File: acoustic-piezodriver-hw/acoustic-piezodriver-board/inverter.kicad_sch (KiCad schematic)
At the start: 35 parts, among them Q1 Si7450DP, Q2 Si7450DP, Q3 Si7450DP, Q4 Si7450DP, U1 UCC27282DR, U2 UCC27282DR

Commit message: [carrier] Added decoupling for DDR (next) Finish power supply
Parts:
- C10: Manufacturing Part Number (none) -> CL05B103KB5NNNC
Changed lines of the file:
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@@
+			)
+		)
+		(property "Manufacturing Part Number" "CL05B103KB5NNNC"
+			(at 125.73 96.52 0)
+			(effects
+				(font
+					(size 1.27 1.27)
+				)
+				(hide yes)
 			)
 		)

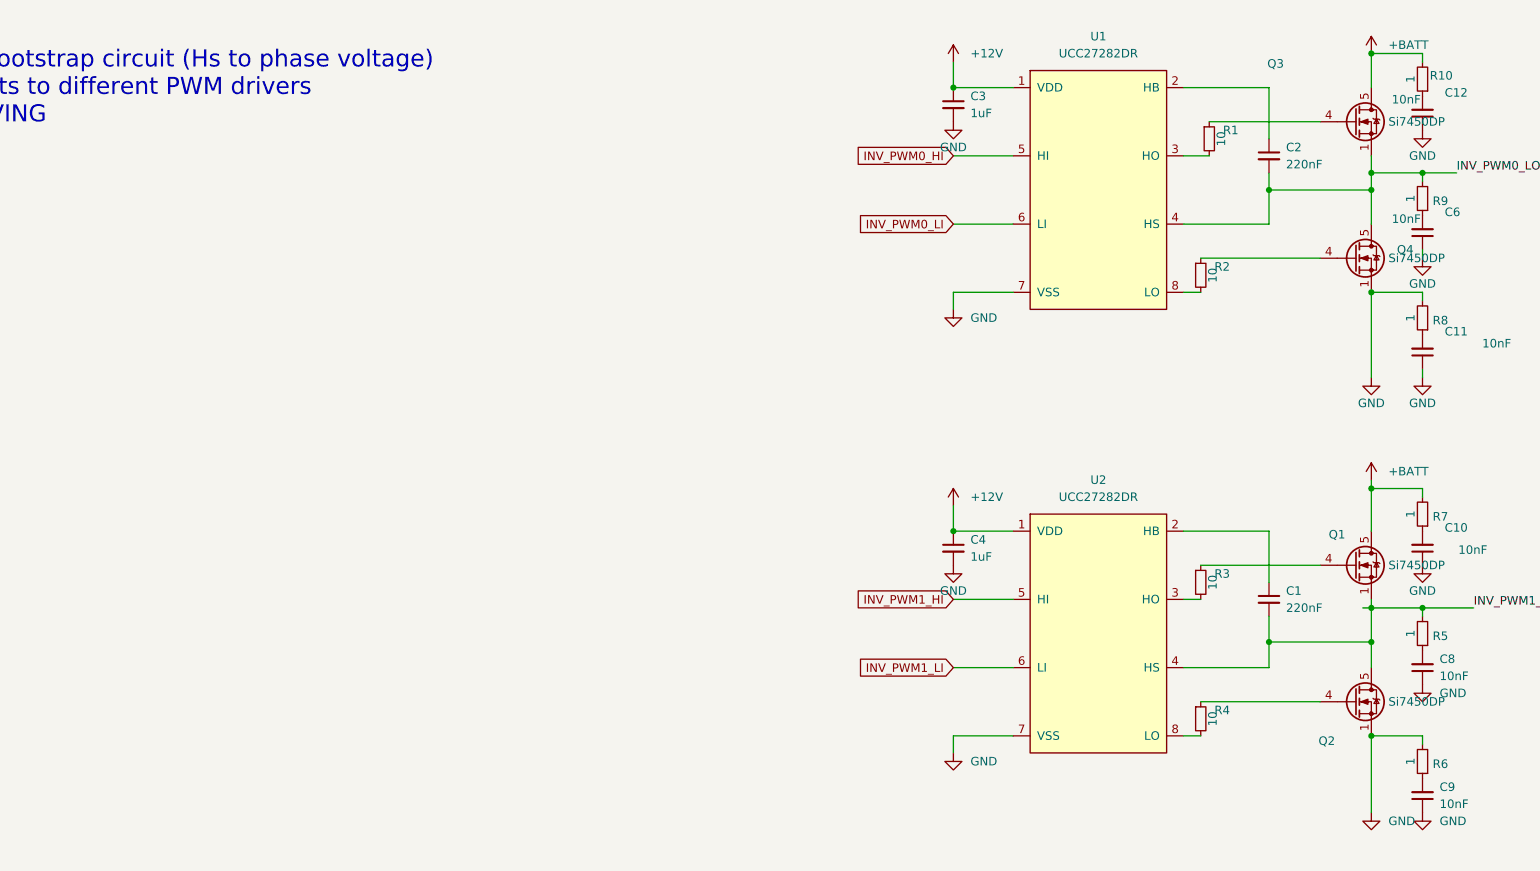
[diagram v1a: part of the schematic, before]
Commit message: [carrier] Added usb power + communication circuitry (next) Connect ADC pins to bank 0, select PWM pins, check connectors for power board
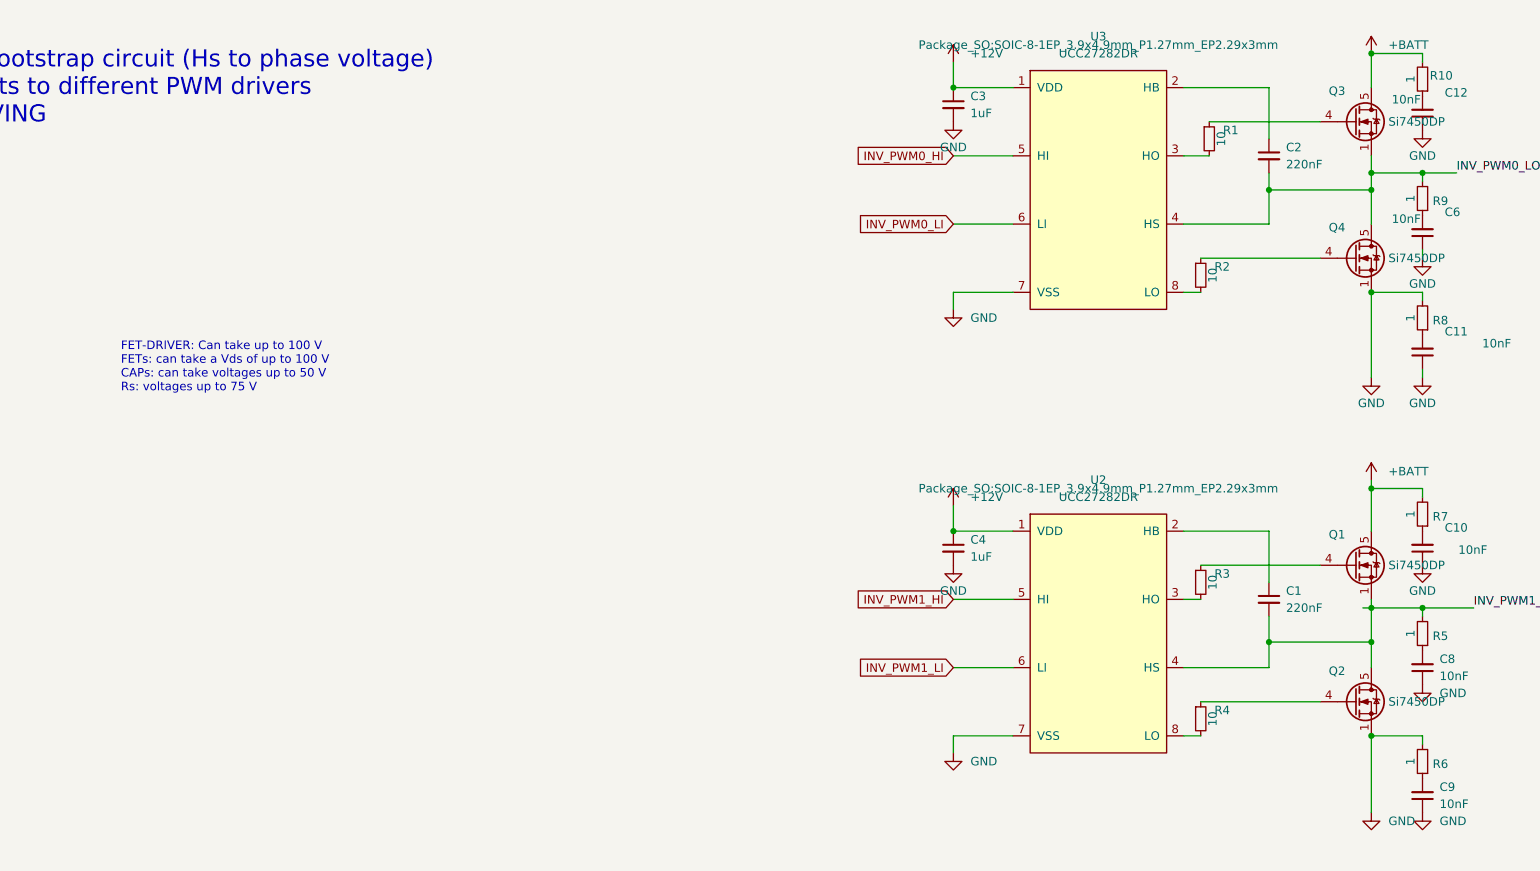
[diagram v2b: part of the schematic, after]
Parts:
- removed U1: UCC27282DR, symbol ucc27282:UCC27282DR
- added U3: UCC27282DR, Package_SO:SOIC-8-1EP_3.9x4.9mm_P1.27mm_EP2.29x3mm, symbol ucc27282:UCC27282DR
- Q1, Q2, Q3, Q4: LCSC Part Number C3289463 -> (none); LPN (none) -> C3289463; MPN (none) -> SI7454FDP-T1-RE3
- U2: footprint (none) -> Package_SO:SOIC-8-1EP_3.9x4.9mm_P1.27mm_EP2.29x3mm; MPN (none) -> UCC27282DR
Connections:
- net +12V: now also U3.1 (VDD)
- net GND: now also U3.7 (VSS)
- net INV_PWM0_HI: now also U3.5 (HI)
- net INV_PWM0_LI: now also U3.6 (LI)
- net INV_PWM0_LOAD: now also U3.4 (HS)
- net at R2.2: now also U3.8 (LO)
- net at C2.1: now also U3.2 (HB)
- net at R1.2: now also U3.3 (HO)
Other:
- note added: "FET-DRIVER: Can take up to 100 V FETs: can take a Vds of up to 100 V CAPs: can take voltages up to 50 V Rs: voltages up to 75 V"

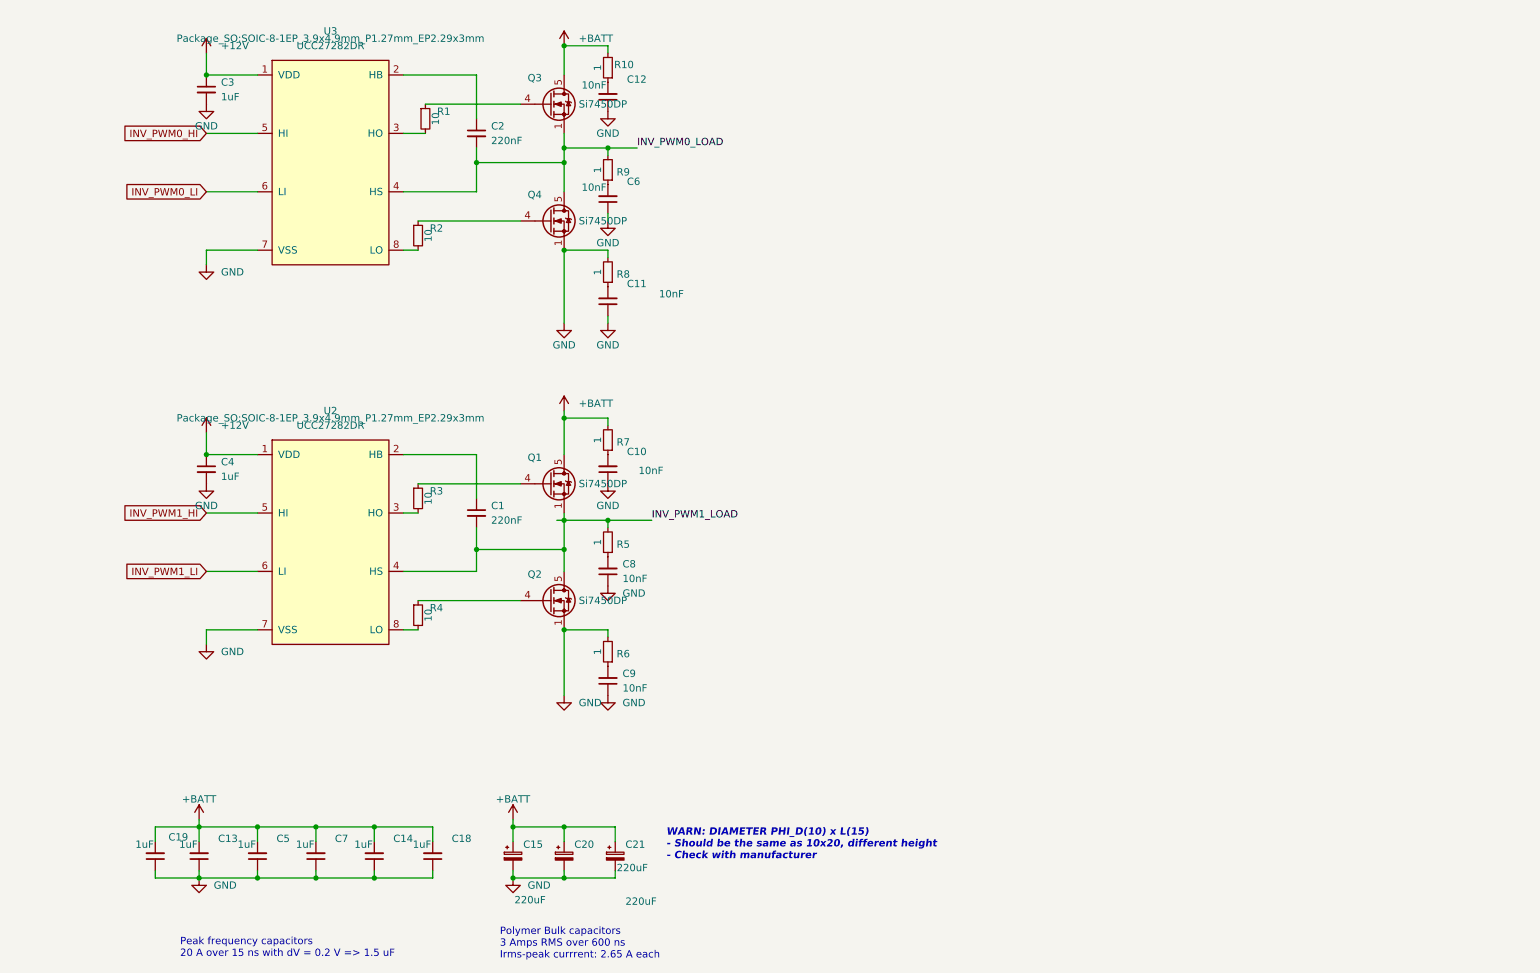
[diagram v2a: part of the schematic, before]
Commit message: [piezodriver] Added piezo-driver board connectors
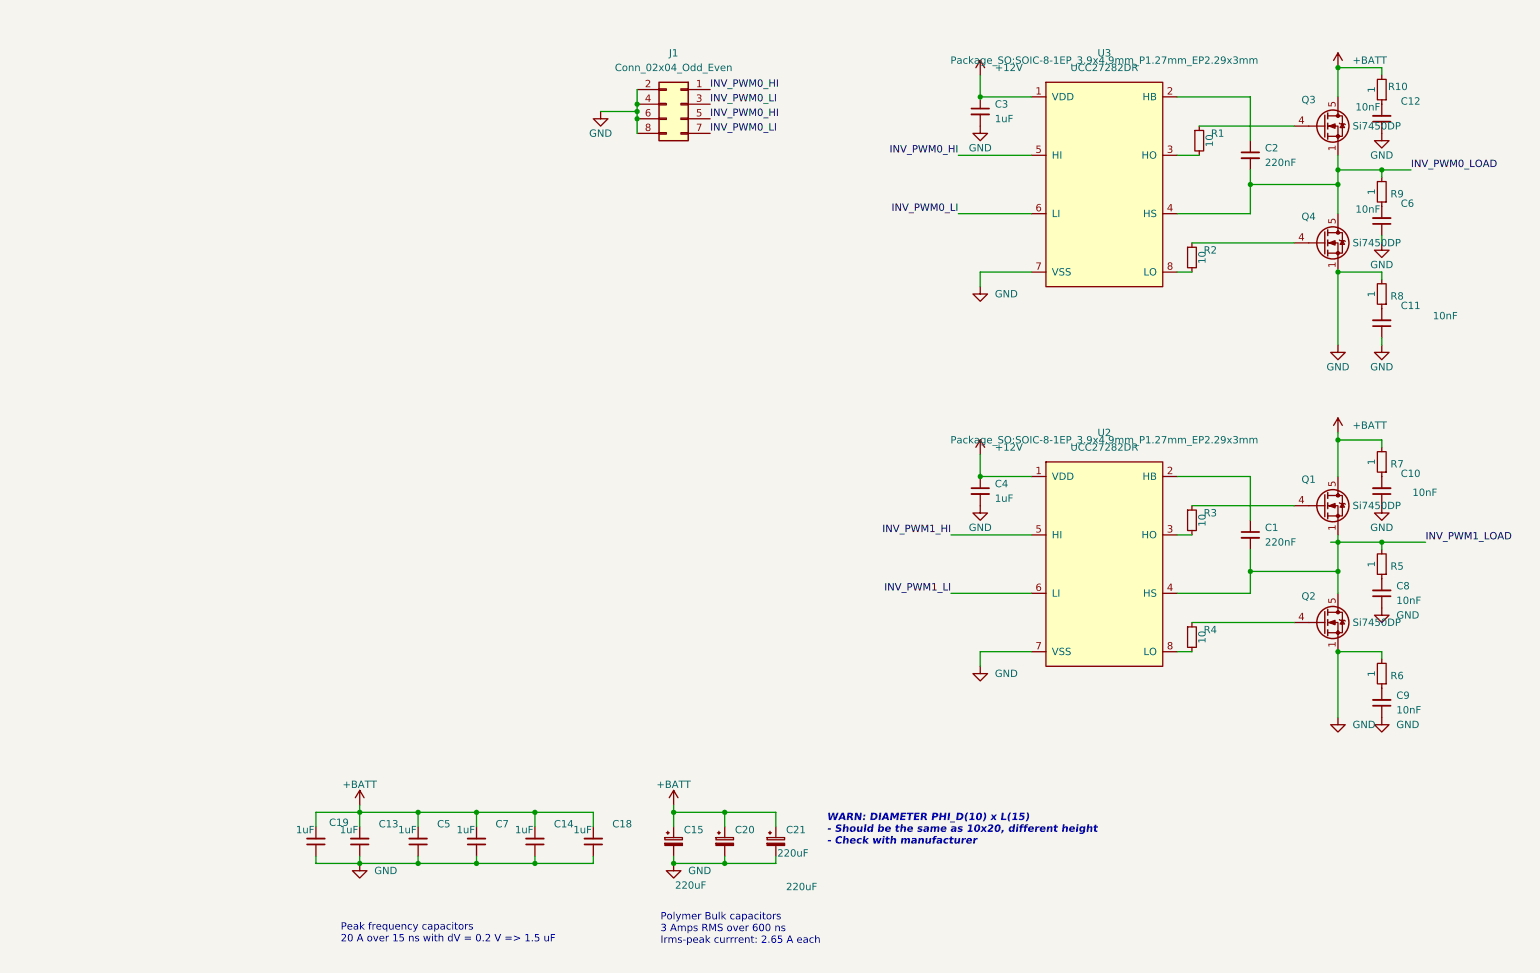
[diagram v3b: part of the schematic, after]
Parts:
- added J1: Conn_02x04_Odd_Even, Connector_PinHeader_2.54mm:PinHeader_2x04_P2.54mm_Horizontal, symbol Connector_Generic:Conn_02x04_Odd_Even
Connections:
- net GND: now also J1.2 (Pin_2), J1.4 (Pin_4), J1.6 (Pin_6), J1.8 (Pin_8)
- net INV_PWM0_HI: now also J1.1 (Pin_1), J1.5 (Pin_5)
- net INV_PWM0_LI: now also J1.3 (Pin_3), J1.7 (Pin_7)
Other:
- moved on the sheet: C1, C10, C11, C12, C13, C14, C15, C18, C19, C2, C20, C21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

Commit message: [driver] added components to sepic, added notes
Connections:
- net +12V renamed +10V
- net +BATT renamed +VDC
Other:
- note added: "Inverter voltage not necessarily equal to input voltage!"

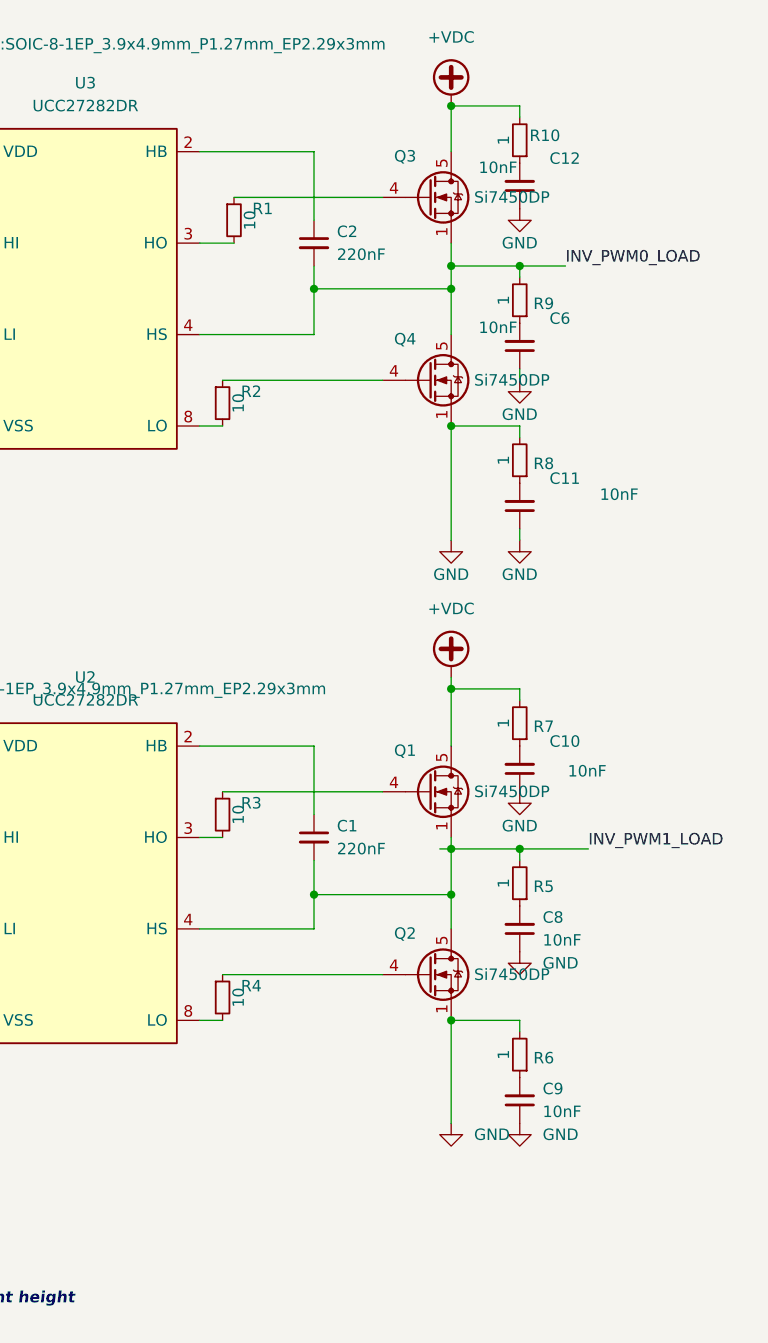
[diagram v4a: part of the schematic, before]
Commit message: [piezodriver] Added X7R input capacitor, add input and output capacitance of 40-100 uF
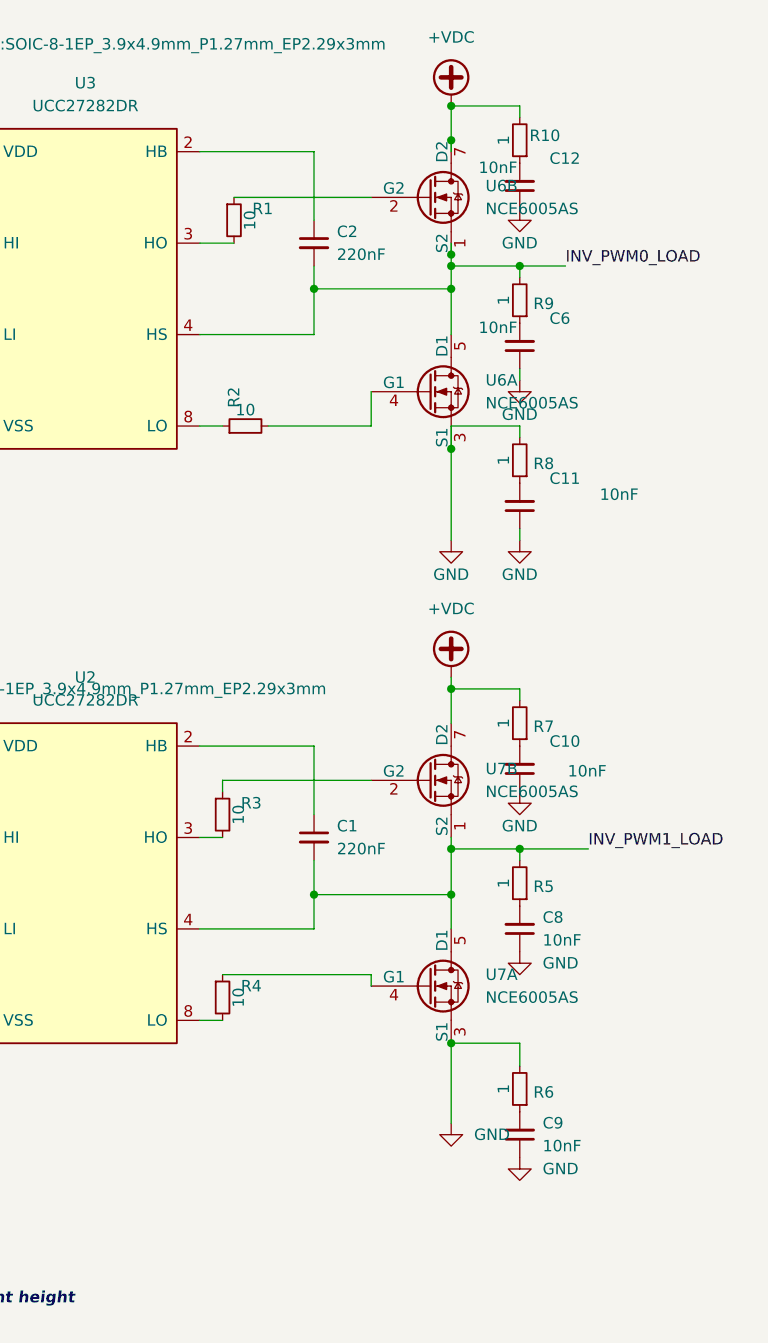
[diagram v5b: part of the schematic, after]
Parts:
- removed Q1, Q2, Q3, Q4: Si7450DP, Package_SO:PowerPAK_SO-8_Single, symbol Transistor_FET:Si7450DP
- added U6: NCE6005AS, Package_SO:SOIC-8_3.9x4.9mm_P1.27mm, symbol custom_mosfet:NCE6005AS
- added U7: NCE6005AS, symbol custom_mosfet:NCE6005AS
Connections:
- net +VDC: now also U6.7 (D2), U6.8 (D2), U7.7 (D2), U7.8 (D2)
- net GND: now also U6.3 (S1), U7.3 (S1)
- net INV_PWM0_LOAD: now also U6.1 (S2), U6.5 (D1), U6.6 (D1)
- net INV_PWM1_LOAD: now also U7.1 (S2), U7.5 (D1), U7.6 (D1)
- net at R3.1: now also U7.2 (G2)
- net at R4.1: now also U7.4 (G1)
- net at R2.1: now also U3.8 (LO)
- net at R2.2: now also U6.4 (G1); no longer U3.8 (LO)
- net at R1.1: now also U6.2 (G2)
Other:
- moved on the sheet: C9, R2, R6

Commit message: [carrier] Reordered carrier board (next) add magnetics to adc differential and ethernet instead of capacitors - SRF is too low
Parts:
- added D4: SS510, Diode_SMD:D_SMA, symbol Device:D_Schottky_Small
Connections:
- net +VDC: now also D4.1 (K)
- net INV_PWM0_LOAD renamed INV_LOAD0
- net INV_PWM1_LOAD renamed INV_LOAD1
- new net +BATT: D4.2 (A)
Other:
- note added: "BOOST BYPASS"
- note added: "DECOUPLING AND BULK"
- note added: "INVERTER"
- note added: "If boost is inactive -> directly pass input to inverter"
- note added: "Notes: - Make sure to correctly connect the bootstrap circuit (Hs to phase voltage) - Make sure to connect all 4 PWM inputs to different PWM drivers => ENSURE DEAD TIME WHEN DRIVING FET-DRIVER: Can take up to 100 V FETs: can take a Vds of up to 100 V CAPs: can take voltages up to 50 V Rs: voltages up to 75 V"
- note added: "PWM CONNECTORS"
- note removed: "FET-DRIVER: Can take up to 100 V FETs: can take a Vds of up to 100 V CAPs: can take voltages up to 50 V Rs: voltages up to 75 V"
- note removed: "Notes: - Make sure to correctly connect the bootstrap circuit (Hs to phase voltage) - Make sure to connect all 4 PWM inputs to different PWM drivers => ENSURE DEAD TIME WHEN DRIVING"
- moved on the sheet: C13, C14, C15, C18, C19, C20, C21, C5, C7, J1
